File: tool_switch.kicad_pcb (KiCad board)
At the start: 2 copper layers, 14 parts, among them P1 CONN_2, P2 CONN_2, P3 CONN_2, P4 CONN_2, P5 CONN_4, Q1 BD578, U1 PC817

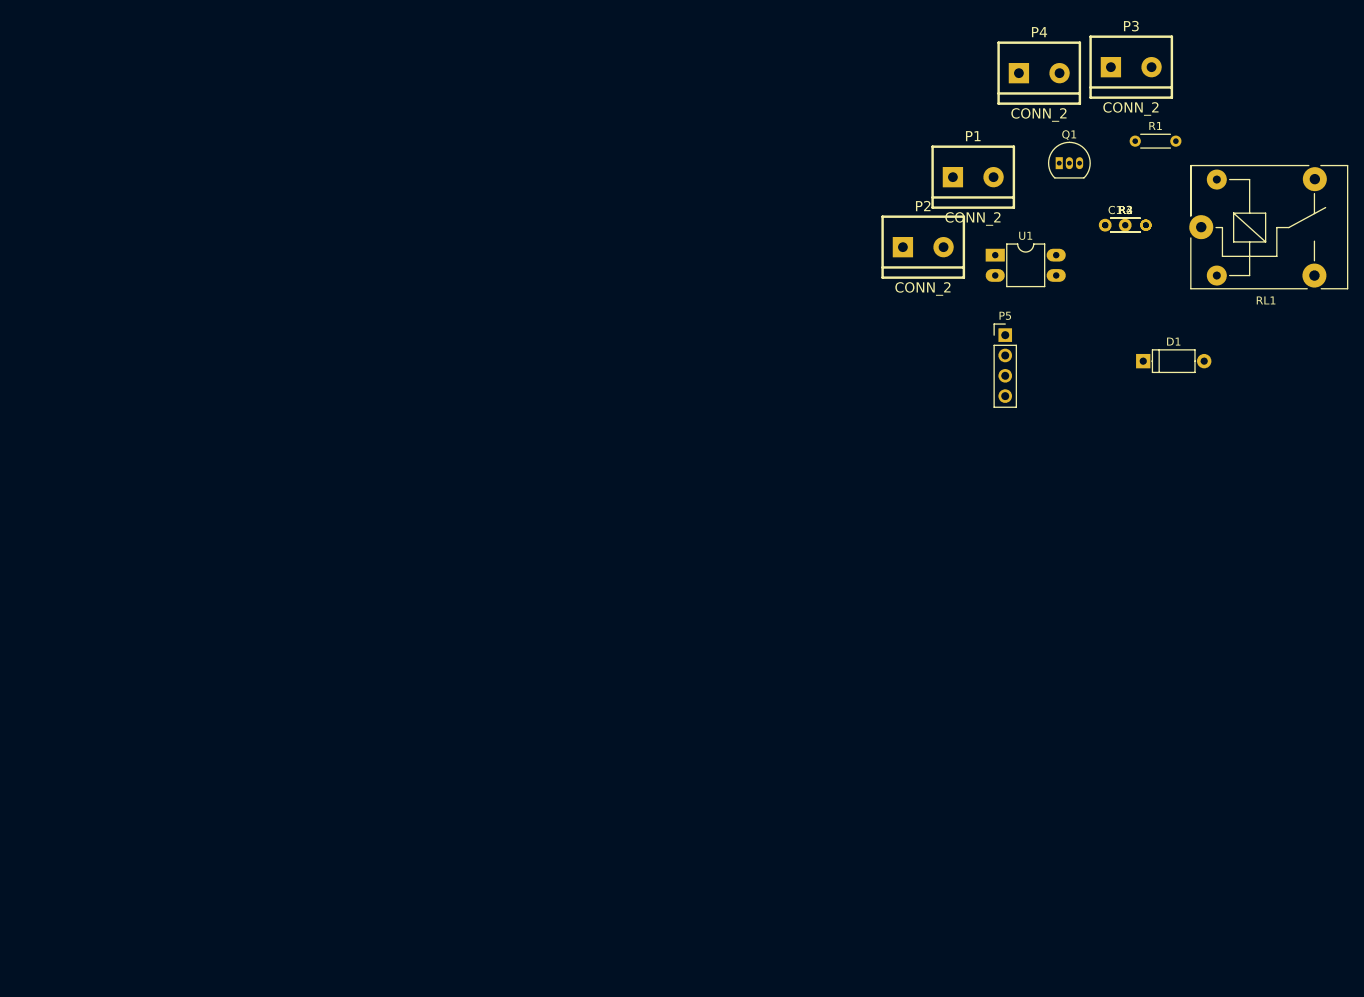
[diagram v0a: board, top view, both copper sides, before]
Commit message: added pcb layout
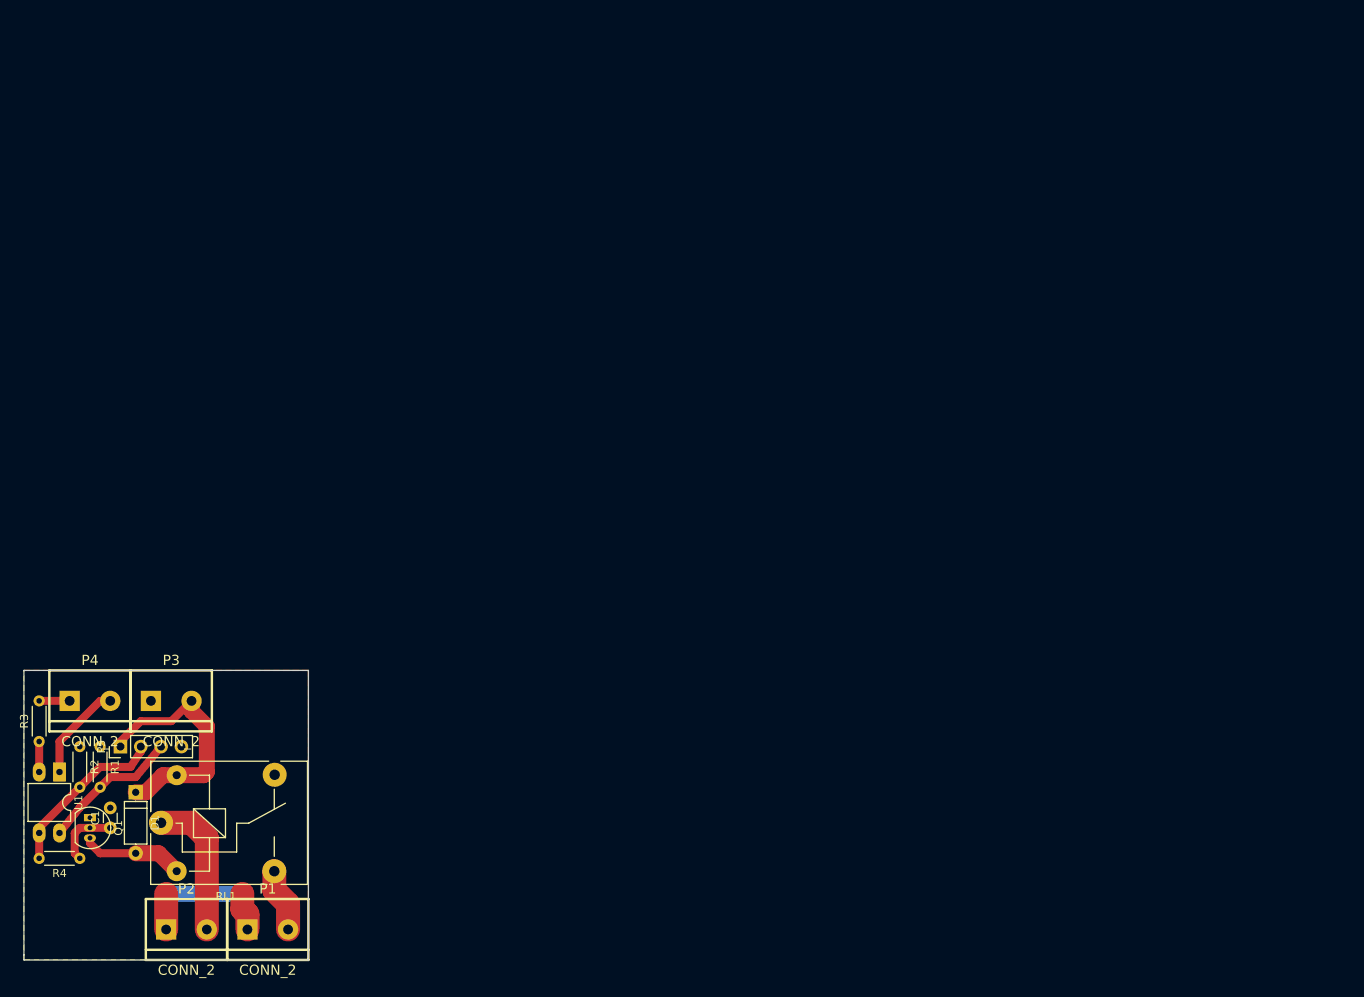
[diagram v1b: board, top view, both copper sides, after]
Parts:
- RL1: value FINDER-36.11.4001 -> G5Q-2
- moved R4 150.6 mm to (20.3, 184.2), turned to 180 degrees
- moved R1 149.9 mm to (22.9, 170.2), turned to 270 degrees
- moved RL1 149.8 mm to (30.5, 179.7)
- moved R3 148.1 mm to (15.2, 169.5), turned to 90 degrees
- moved Q1 146.2 mm to (21.6, 179.1), turned to 270 degrees
- moved C1 145.4 mm to (24.1, 180.3), turned to 90 degrees
- moved R2 143.8 mm to (20.3, 170.2), turned to 270 degrees
- moved P3 143.8 mm to (31.8, 164.5)
- moved P4 142.3 mm to (21.6, 164.5)
- moved D1 137.0 mm to (27.3, 175.9), turned to 270 degrees
- moved U1 133.6 mm to (17.8, 173.4), turned to 270 degrees
- moved P1 128.9 mm to (43.8, 193.0)
- moved P2 125.5 mm to (33.7, 193.0)
- moved P5 122.0 mm to (25.4, 170.2), turned to 90 degrees
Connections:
- P1 pad 2: (no net) -> Ai
- P2 pad 2: (no net) -> Ao
- RL1 pad 1: (no net) -> Ao
- RL1 pad 2: (no net) -> Net-(D1-Pad2)
- RL1 pad 3: (no net) -> Ai
- RL1 pad 5: (no net) -> +9V
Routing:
- net +9V: track 0.00 -> 31.8 mm
- net opt1: track 0.00 -> 21.3 mm
- net Ao: track 0.00 -> 17.9 mm
- net opt2: track 0.00 -> 17.6 mm
- net Net-(D1-Pad2): track 0.00 -> 12.9 mm
- net Net-(P4-Pad2): track 0.00 -> 12.3 mm
- net (no net): track 0.00 -> 9.53 mm
- net B0: track 0.00 -> 9.15 mm
- net Net-(C1-Pad1): track 0.00 -> 8.15 mm
- net Ai: track 0.00 -> 8.00 mm
- net Net-(R3-Pad1): track 0.00 -> 3.81 mm
- net Net-(P4-Pad1): track 0.00 -> 3.81 mm
- added copper zone on F.Cu, net GND
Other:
- board outline added: 35.6 x 36.2 mm
- net class Default: trace_width 0.25 -> 2
- net class power added: clearance 0.1, trace_width 3, via_dia 0.6, via_drill 0.4
